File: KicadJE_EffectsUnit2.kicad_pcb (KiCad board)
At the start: 2 copper layers, 100 x 100 mm, 103 parts, among them J201 In_1, J202 In 2, J203 Out 1, J204 Out 2, J205 Out Final, J301 Conn_01x09_Male, J302 Conn_01x09_Male, J401 Conn_01x09_Male, J402 Conn_01x09_Male, P201 Doepfer_Power_10pin, P301 Doepfer_Power_10pin, SW201 Out 1, SW202 In or cascade, SW203 Out 2 FB, SW204 In or cascade, SW205 HI/LO, U201 TL072, U202 TL072, U401 TL072, U402 TL072

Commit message: 3D messing around
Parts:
- moved U402 60.2 mm to (120.0, 125.8), turned to 90 degrees
- moved C402 58.6 mm to (125.8, 73.1), turned to 90 degrees
- moved U401 55.5 mm to (120.0, 75.0), turned to 90 degrees
- moved C406 52.5 mm to (125.8, 77.0), turned to 90 degrees
- moved C405 47.9 mm to (125.0, 127.8), turned to 90 degrees
- moved C403 42.4 mm to (125.0, 123.8), turned to 90 degrees
- moved J402 1.42 mm to (128.0, 136.1)
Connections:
- C301 pad 1: -12V -> /angled_panel/-12V_1
- C301 pad 2: GND -> /angled_panel/GND_1
- C302 pad 1: GND -> /angled_panel/GND_1
- C302 pad 2: -12V -> /angled_panel/-12V_1
- C303 pad 1: GND -> /angled_panel/GND_1
- C303 pad 2: -12V -> /angled_panel/-12V_1
- C304 pad 1: GND -> /angled_panel/GND_1
- C304 pad 2: +12V -> /angled_panel/+12V_1
- C305 pad 1: +12V -> /angled_panel/+12V_1
- C305 pad 2: GND -> /angled_panel/GND_1
- C306 pad 1: +12V -> /angled_panel/+12V_1
- C306 pad 2: GND -> /angled_panel/GND_1
- C402 pad 2: Net-(C402-Pad2) -> +12V
- C403 pad 2: Net-(C402-Pad2) -> +12V
- C405 pad 1: Net-(C405-Pad1) -> -12V
- C406 pad 1: Net-(C405-Pad1) -> -12V
- D301 pad 1: -12V -> /angled_panel/-12V_1
- D301 pad 2: GND -> /angled_panel/GND_1
- D302 pad 1: GND -> /angled_panel/GND_1
- D302 pad 2: +12V -> /angled_panel/+12V_1
- J301 pad 1: /KicadJE_EU8_Dist/POT2_L -> /angled_panel/POT2_L
- J301 pad 2: /KicadJE_EU8_Dist/POT2_C -> /angled_panel/POT2_C
- J301 pad 3: /KicadJE_EU8_Dist/POT2_H -> /angled_panel/POT2_H
- J301 pad 4: -12V -> /angled_panel/-12V_1
- J301 pad 5: GND -> /angled_panel/GND_1
- J301 pad 6: +12V -> /angled_panel/+12V_1
- J301 pad 7: /KicadJE_EU8_Dist/POT1_L -> /angled_panel/POT1_L
- J301 pad 8: /KicadJE_EU8_Dist/POT1_C -> /angled_panel/POT1_C
- J301 pad 9: /KicadJE_EU8_Dist/POT1_H -> /angled_panel/POT1_H
- J302 pad 1: /KicadJE_EU8_Dist/POT4_L -> /angled_panel/POT4_L
- J302 pad 2: /KicadJE_EU8_Dist/POT4_C -> /angled_panel/POT4_C
- J302 pad 3: /KicadJE_EU8_Dist/POT4_H -> /angled_panel/POT4_H
- J302 pad 4: -12V -> /angled_panel/-12V_1
- J302 pad 5: GND -> /angled_panel/GND_1
- J302 pad 6: +12V -> /angled_panel/+12V_1
- J302 pad 7: /KicadJE_EU8_Dist/POT3_L -> /angled_panel/POT3_L
- J302 pad 8: /KicadJE_EU8_Dist/POT3_C -> /angled_panel/POT3_C
- J302 pad 9: /KicadJE_EU8_Dist/POT3_H -> /angled_panel/POT3_H
- J401 pad 1: /KicadJE_EU8_Dist/POT2_L -> (no net)
- J401 pad 2: /KicadJE_EU8_Dist/POT2_C -> (no net)
- J401 pad 3: /KicadJE_EU8_Dist/POT2_H -> (no net)
- J401 pad 7: /KicadJE_EU8_Dist/POT1_L -> (no net)
- J401 pad 8: /KicadJE_EU8_Dist/POT1_C -> (no net)
- J401 pad 9: /KicadJE_EU8_Dist/POT1_H -> (no net)
- J402 pad 1: /KicadJE_EU8_Dist/POT4_L -> (no net)
- J402 pad 2: /KicadJE_EU8_Dist/POT4_C -> (no net)
- J402 pad 3: /KicadJE_EU8_Dist/POT4_H -> (no net)
- J402 pad 7: /KicadJE_EU8_Dist/POT3_L -> (no net)
- J402 pad 8: /KicadJE_EU8_Dist/POT3_C -> (no net)
- J402 pad 9: /KicadJE_EU8_Dist/POT3_H -> (no net)
- P301 pad 1: -12V -> /angled_panel/-12V_1
- P301 pad 10: +12V -> /angled_panel/+12V_1
- P301 pad 2: -12V -> /angled_panel/-12V_1
- P301 pad 3: GND -> /angled_panel/GND_1
- P301 pad 4: GND -> /angled_panel/GND_1
- P301 pad 5: GND -> /angled_panel/GND_1
- P301 pad 6: GND -> /angled_panel/GND_1
- P301 pad 7: GND -> /angled_panel/GND_1
- P301 pad 8: GND -> /angled_panel/GND_1
- P301 pad 9: +12V -> /angled_panel/+12V_1
- RV301 pad 1: /KicadJE_EU8_Dist/POT1_L -> /angled_panel/POT1_L
- RV301 pad 2: /KicadJE_EU8_Dist/POT1_C -> /angled_panel/POT1_C
- RV301 pad 3: /KicadJE_EU8_Dist/POT1_H -> /angled_panel/POT1_H
- RV302 pad 1: /KicadJE_EU8_Dist/POT2_L -> /angled_panel/POT2_L
- RV302 pad 2: /KicadJE_EU8_Dist/POT2_C -> /angled_panel/POT2_C
- RV302 pad 3: /KicadJE_EU8_Dist/POT2_H -> /angled_panel/POT2_H
- RV303 pad 1: /KicadJE_EU8_Dist/POT3_L -> /angled_panel/POT3_L
- RV303 pad 2: /KicadJE_EU8_Dist/POT3_C -> /angled_panel/POT3_C
- RV303 pad 3: /KicadJE_EU8_Dist/POT3_H -> /angled_panel/POT3_H
- RV304 pad 1: /KicadJE_EU8_Dist/POT4_L -> /angled_panel/POT4_L
- RV304 pad 2: /KicadJE_EU8_Dist/POT4_C -> /angled_panel/POT4_C
- RV304 pad 3: /KicadJE_EU8_Dist/POT4_H -> /angled_panel/POT4_H
- U401 pad 4: Net-(C405-Pad1) -> -12V
- U401 pad 8: Net-(C402-Pad2) -> +12V
- U402 pad 4: Net-(C405-Pad1) -> -12V
- U402 pad 8: Net-(C402-Pad2) -> +12V
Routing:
- net /angled_panel/+12V_1: track 0.00 -> 116.8 mm, vias 0 -> 4
- net +12V: track 116.8 -> 12.8 mm, vias 4 -> 0
- net /angled_panel/-12V_1: track 0.00 -> 83.5 mm
- net -12V: track 83.5 -> 23.2 mm
- net /angled_panel/GND_1: track 0.00 -> 36.1 mm, vias 0 -> 50
- net GND: track 94.2 -> 72.1 mm, vias 133 -> 84
- net /angled_panel/POT2_L: track 0.00 -> 11.2 mm
- net /KicadJE_EU8_Dist/POT2_L: track 11.2 -> 0.00 mm
- net /angled_panel/POT3_H: track 0.00 -> 10.9 mm
- net /KicadJE_EU8_Dist/POT3_H: track 10.9 -> 0.00 mm
- net /angled_panel/POT2_C: track 0.00 -> 8.74 mm
- net /KicadJE_EU8_Dist/POT2_C: track 8.74 -> 0.00 mm
- net /angled_panel/POT3_C: track 0.00 -> 8.42 mm
- net /KicadJE_EU8_Dist/POT3_C: track 8.42 -> 0.00 mm
- net /angled_panel/POT2_H: track 0.00 -> 6.28 mm
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- added copper zone on B.Cu, net /angled_panel/GND_1
- added copper zone on F.Cu, net /angled_panel/GND_1
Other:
- outline, holes or cut-outs redrawn

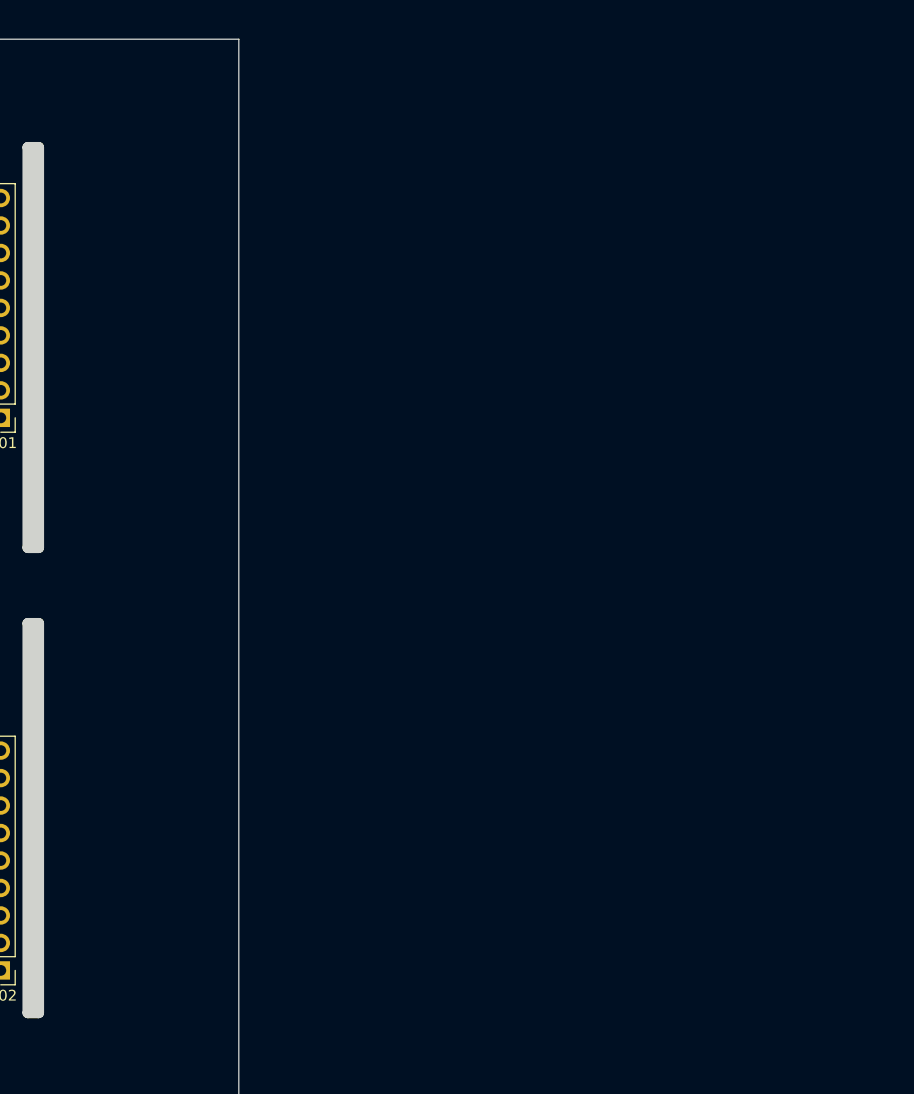
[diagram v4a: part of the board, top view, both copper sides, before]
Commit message: PCB dist 2 placement of face panel
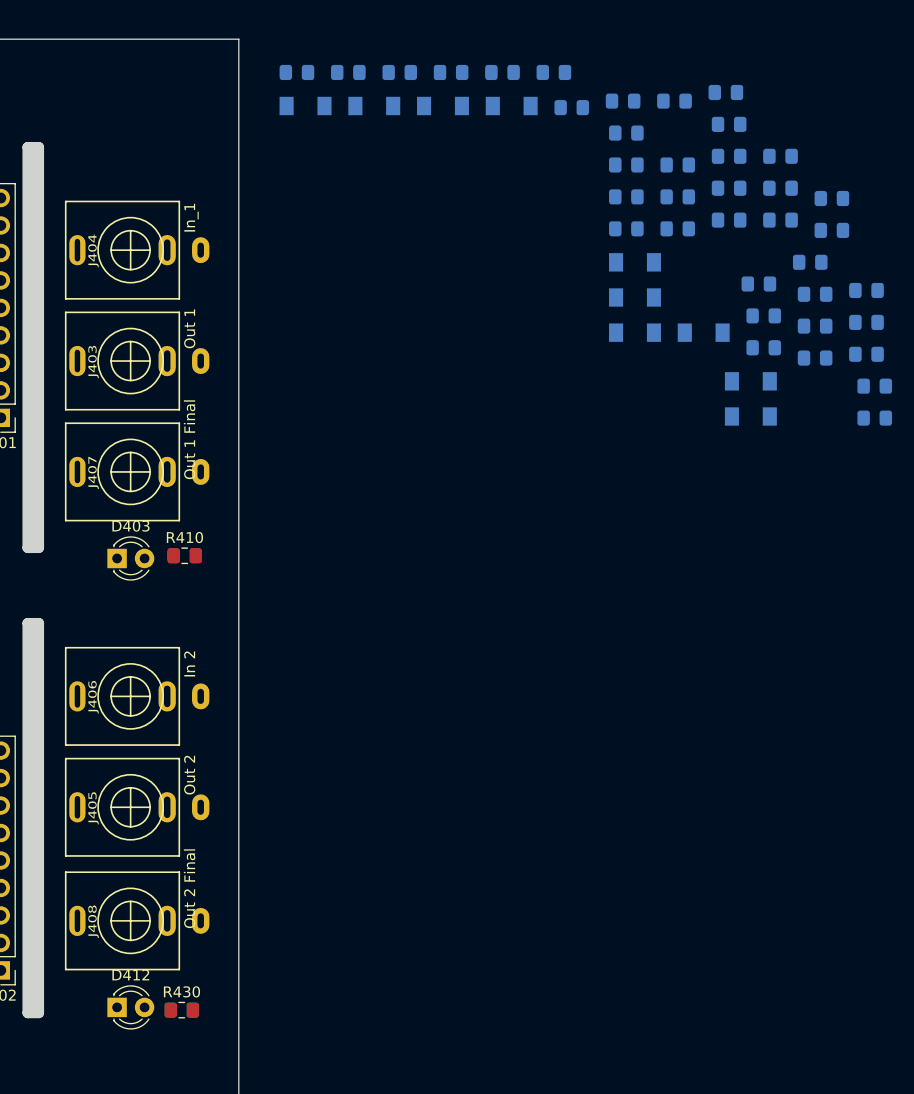
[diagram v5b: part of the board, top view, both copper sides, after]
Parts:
- added C401: 10n, Capacitor_SMD:C_0805_2012Metric_Pad1.15x1.40mm_HandSolder, B.Cu at (198.5, 75.6)
- added C404: 10n, Capacitor_SMD:C_0805_2012Metric_Pad1.15x1.40mm_HandSolder, B.Cu at (164.9, 53.1)
- added C407: 10n, Capacitor_SMD:C_0805_2012Metric_Pad1.15x1.40mm_HandSolder, B.Cu at (169.6, 53.1)
- added C408: 10n, Capacitor_SMD:C_0805_2012Metric_Pad1.15x1.40mm_HandSolder, B.Cu at (198.5, 78.5)
- added C409: 1u, Capacitor_SMD:C_0805_2012Metric_Pad1.15x1.40mm_HandSolder, B.Cu at (185.8, 67.5)
- added C410: 1u, Capacitor_SMD:C_0805_2012Metric_Pad1.15x1.40mm_HandSolder, B.Cu at (185.8, 64.6)
- added C411: 1u, Capacitor_SMD:C_0805_2012Metric_Pad1.15x1.40mm_HandSolder, B.Cu at (174.4, 53.1)
- added C412: 1u, Capacitor_SMD:C_0805_2012Metric_Pad1.15x1.40mm_HandSolder, B.Cu at (155.4, 53.1)
- added C413: 1u, Capacitor_SMD:C_0805_2012Metric_Pad1.15x1.40mm_HandSolder, B.Cu at (180.8, 56.3)
- added C414: 1u, Capacitor_SMD:C_0805_2012Metric_Pad1.15x1.40mm_HandSolder, B.Cu at (185.8, 61.6)
- added D401: LL4148, Diode_SMD:D_MiniMELF, B.Cu at (186.6, 77.1)
- added D402: LL4148, Diode_SMD:D_MiniMELF, B.Cu at (168.9, 56.2)
- added D403: LED, LED_THT:LED_D3.0mm, F.Cu at (138.8, 98.0)
- added D404: LL4148, Diode_SMD:D_MiniMELF, B.Cu at (193.0, 77.1)
- added D405: LL4148, Diode_SMD:D_MiniMELF, B.Cu at (156.2, 56.2)
- added D406: LL4148, Diode_SMD:D_MiniMELF, B.Cu at (162.5, 56.2)
- added D407: LL4148, Diode_SMD:D_MiniMELF, B.Cu at (186.6, 73.9)
- added D408: LL4148, Diode_SMD:D_MiniMELF, B.Cu at (175.2, 56.2)
- added D409: LL4148, Diode_SMD:D_MiniMELF, B.Cu at (197.3, 84.9)
- added D410: D_Zener, Diode_SMD:D_MiniMELF, B.Cu at (186.6, 70.6)
- added D411: D_Zener, Diode_SMD:D_MiniMELF, B.Cu at (197.3, 81.6)
- added D412: LED, LED_THT:LED_D3.0mm, F.Cu at (138.8, 139.5)
- added J403: Out 1, AJ-Dropbox-Kicad:PJ301SM, F.Cu at (140.0, 79.8)
- added J404: In_1, AJ-Dropbox-Kicad:PJ301SM, F.Cu at (140.0, 69.5)
- added J405: Out 2, AJ-Dropbox-Kicad:PJ301SM, F.Cu at (140.0, 121.0)
- added J406: In 2, AJ-Dropbox-Kicad:PJ301SM, F.Cu at (140.0, 110.8)
- added J407: Out 1 Final, AJ-Dropbox-Kicad:PJ301SM, F.Cu at (140.0, 90.0)
- added J408: Out 2 Final, AJ-Dropbox-Kicad:PJ301SM, F.Cu at (140.0, 131.5)
- added R401: 1k, Resistor_SMD:R_0805_2012Metric_Pad1.15x1.40mm_HandSolder, B.Cu at (190.6, 67.5)
- added R402: 10k, Resistor_SMD:R_0805_2012Metric_Pad1.15x1.40mm_HandSolder, B.Cu at (208.0, 76.2)
- added R403: 10k, Resistor_SMD:R_0805_2012Metric_Pad1.15x1.40mm_HandSolder, B.Cu at (203.3, 79.5)
- added R404: 1k, Resistor_SMD:R_0805_2012Metric_Pad1.15x1.40mm_HandSolder, B.Cu at (190.6, 64.6)
- added R405: 1k, Resistor_SMD:R_0805_2012Metric_Pad1.15x1.40mm_HandSolder, B.Cu at (198.1, 72.6)
- added R406: 1k, Resistor_SMD:R_0805_2012Metric_Pad1.15x1.40mm_HandSolder, B.Cu at (179.1, 53.1)
- added R407: 10k, Resistor_SMD:R_0805_2012Metric_Pad1.15x1.40mm_HandSolder, B.Cu at (203.3, 76.5)
- added R408: 10k, Resistor_SMD:R_0805_2012Metric_Pad1.15x1.40mm_HandSolder, B.Cu at (208.8, 82.1)
- added R409: 10R, Resistor_SMD:R_0805_2012Metric_Pad1.15x1.40mm_HandSolder, B.Cu at (185.8, 58.7)
- added R410: 1k, Resistor_SMD:R_0805_2012Metric_Pad1.15x1.40mm_HandSolder, F.Cu at (145.0, 97.8)
- added R411: 1k, Resistor_SMD:R_0805_2012Metric_Pad1.15x1.40mm_HandSolder, B.Cu at (190.6, 61.6)
- added R412: 10k, Resistor_SMD:R_0805_2012Metric_Pad1.15x1.40mm_HandSolder, B.Cu at (195.3, 66.7)
- added R413: 10k, Resistor_SMD:R_0805_2012Metric_Pad1.15x1.40mm_HandSolder, B.Cu at (185.5, 55.7)
- added R414: 1k, Resistor_SMD:R_0805_2012Metric_Pad1.15x1.40mm_HandSolder, B.Cu at (208.0, 79.1)
- added R415: 10k, Resistor_SMD:R_0805_2012Metric_Pad1.15x1.40mm_HandSolder, B.Cu at (203.3, 73.6)
- added R416: 10k, Resistor_SMD:R_0805_2012Metric_Pad1.15x1.40mm_HandSolder, B.Cu at (208.8, 85.0)
- added R417: 1k, Resistor_SMD:R_0805_2012Metric_Pad1.15x1.40mm_HandSolder, B.Cu at (160.1, 53.1)
- added R418: Open, Resistor_SMD:R_0805_2012Metric_Pad1.15x1.40mm_HandSolder, B.Cu at (195.3, 63.8)
- added R419: Open, Resistor_SMD:R_0805_2012Metric_Pad1.15x1.40mm_HandSolder, B.Cu at (202.8, 70.6)
- added R420: 1k, Resistor_SMD:R_0805_2012Metric_Pad1.15x1.40mm_HandSolder, B.Cu at (200.1, 66.7)
- added R421: 10R, Resistor_SMD:R_0805_2012Metric_Pad1.15x1.40mm_HandSolder, B.Cu at (190.3, 55.7)
- added R422: 0R, Resistor_SMD:R_0805_2012Metric_Pad1.15x1.40mm_HandSolder, B.Cu at (195.3, 60.8)
- added R423: 0R, Resistor_SMD:R_0805_2012Metric_Pad1.15x1.40mm_HandSolder, B.Cu at (208.0, 73.2)
- added R424: 10k, Resistor_SMD:R_0805_2012Metric_Pad1.15x1.40mm_HandSolder, B.Cu at (200.1, 63.8)
- added R425: OPEN, Resistor_SMD:R_0805_2012Metric_Pad1.15x1.40mm_HandSolder, B.Cu at (204.8, 67.7)
- added R426: 10k, Resistor_SMD:R_0805_2012Metric_Pad1.15x1.40mm_HandSolder, B.Cu at (195.3, 57.9)
- added R427: OPEN, Resistor_SMD:R_0805_2012Metric_Pad1.15x1.40mm_HandSolder, B.Cu at (200.1, 60.8)
- added R428: 100k, Resistor_SMD:R_0805_2012Metric_Pad1.15x1.40mm_HandSolder, B.Cu at (204.8, 64.7)
- added R429: 100k, Resistor_SMD:R_0805_2012Metric_Pad1.15x1.40mm_HandSolder, B.Cu at (195.0, 54.9)
- added R430: 1k, Resistor_SMD:R_0805_2012Metric_Pad1.15x1.40mm_HandSolder, F.Cu at (144.7, 139.8)
- R209, R214: value 150R -> 680R
- R216: value 1k -> 10R
- R220: value 150R -> 1k
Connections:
- J401 pad 1: (no net) -> /KicadJE_EU8_Dist/POT2_L
- J401 pad 2: (no net) -> /KicadJE_EU8_Dist/POT2_C
- J401 pad 3: (no net) -> /KicadJE_EU8_Dist/POT2_C
- J401 pad 7: (no net) -> /KicadJE_EU8_Dist/POT1_L
- J401 pad 8: (no net) -> /KicadJE_EU8_Dist/POT1_C
- J401 pad 9: (no net) -> /KicadJE_EU8_Dist/POT1_C
- J402 pad 1: (no net) -> /KicadJE_EU8_Dist/POT4_L
- J402 pad 2: (no net) -> /KicadJE_EU8_Dist/POT4_C
- J402 pad 3: (no net) -> /KicadJE_EU8_Dist/POT4_C
- J402 pad 7: (no net) -> /KicadJE_EU8_Dist/POT3_L
- J402 pad 8: (no net) -> /KicadJE_EU8_Dist/POT3_C
- J402 pad 9: (no net) -> /KicadJE_EU8_Dist/POT3_C
- U401 pad 1: (no net) -> Net-(R405-Pad2)
- U401 pad 2: (no net) -> /KicadJE_EU8_Dist/POT1_L
- U401 pad 3: (no net) -> Net-(R407-Pad1)
- U401 pad 5: (no net) -> Net-(R408-Pad1)
- U401 pad 6: (no net) -> /KicadJE_EU8_Dist/POT2_L
- U401 pad 7: (no net) -> Net-(R404-Pad2)
- U402 pad 1: (no net) -> /KicadJE_EU8_Dist/POT3_C
- U402 pad 2: (no net) -> Net-(C407-Pad1)
- U402 pad 3: (no net) -> Net-(R418-Pad1)
- U402 pad 5: (no net) -> Net-(R419-Pad1)
- U402 pad 6: (no net) -> Net-(R413-Pad2)
- U402 pad 7: (no net) -> /KicadJE_EU8_Dist/POT4_C

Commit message: Update KicadJE_EffectsUnit2.kicad_pcb
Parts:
- moved R430 4.46 mm to (149.0, 138.5), turned to 90 degrees
- moved R410 4.07 mm to (149.0, 97.0), turned to 90 degrees
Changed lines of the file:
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@@
   )
   (module Resistor_SMD:R_0805_2012Metric_Pad1.15x1.40mm_HandSolder (layer F.Cu)
-    (at 145 97.75)
-    (descr "Resistor SMD 0805 (2012 Metric), square (rectangular) end terminal, IPC_7351 nominal with elongated pad for handsoldering. (Body size source: https://docs.google.com/spreadsheets/d/1BsfQQcO9C6DZCsRaXUlFlo91Tg2WpOkGARC1WS5S8t0/edit?usp=sharing), generated with kicad-footprint-generator")
-    (tags "resistor handsolder")
-    (attr smd)
-    (fp_text reference R410 (at 0 -1.65) (layer F.SilkS)
+    (at 149 96.975 90)
+    (descr "Resistor SMD 0805 (2012 Metric), square (rectangular) end terminal, IPC_7351 nominal with elongated pad for handsoldering. (Body size source: https://docs.google.com/spreadsheets/d/1BsfQQcO9C6DZCsRaXUlFlo91Tg2WpOkGARC1WS5S8t0/edit?usp=sharing), generated with kicad-footprint-generator")
+    (tags "resistor handsolder")
+    (attr smd)
+    (fp_text reference R410 (at 0 -1.65 90) (layer F.SilkS)
       (effects (font (size 1 1) (thickness 0.15)))
     )
-    (fp_text value 1k (at 0 1.65) (layer F.Fab)
+    (fp_text value 1k (at -3 0 90) (layer F.Fab)
       (effects (font (size 1 1) (thickness 0.15)))
     )
-    (fp_text user %R (at 0 0) (layer F.Fab)
+    (fp_text user %R (at 0 0 90) (layer F.Fab)
       (effects (font (size 0.5 0.5) (thickness 0.08)))
     )
@@
     (fp_line (start -1 -0.6) (end 1 -0.6) (layer F.Fab) (width 0.1))
     (fp_line (start -1 0.6) (end -1 -0.6) (layer F.Fab) (width 0.1))
-    (pad 2 smd roundrect (at 1.025 0) (size 1.15 1.4) (layers F.Cu F.Paste F.Mask) (roundrect_rratio 0.217391)
+    (pad 2 smd roundrect (at 1.025 0 90) (size 1.15 1.4) (layers F.Cu F.Paste F.Mask) (roundrect_rratio 0.217391)
       (net 81 "Net-(R404-Pad2)"))
-    (pad 1 smd roundrect (at -1.025 0) (size 1.15 1.4) (layers F.Cu F.Paste F.Mask) (roundrect_rratio 0.217391)
+    (pad 1 smd roundrect (at -1.025 0 90) (size 1.15 1.4) (layers F.Cu F.Paste F.Mask) (roundrect_rratio 0.217391)
       (net 70 "Net-(D403-Pad2)"))
     (model ${KISYS3DMOD}/Resistor_SMD.3dshapes/R_0805_2012Metric.wrl
@@
   )
   (module Resistor_SMD:R_0805_2012Metric_Pad1.15x1.40mm_HandSolder (layer F.Cu)
-    (at 144.725 139.75)
-    (descr "Resistor SMD 0805 (2012 Metric), square (rectangular) end terminal, IPC_7351 nominal with elongated pad for handsoldering. (Body size source: https://docs.google.com/spreadsheets/d/1BsfQQcO9C6DZCsRaXUlFlo91Tg2WpOkGARC1WS5S8t0/edit?usp=sharing), generated with kicad-footprint-generator")
-    (tags "resistor handsolder")
-    (attr smd)
-    (fp_text reference R430 (at 0 -1.65) (layer F.SilkS)
+    (at 149 138.475 90)
+    (descr "Resistor SMD 0805 (2012 Metric), square (rectangular) end terminal, IPC_7351 nominal with elongated pad for handsoldering. (Body size source: https://docs.google.com/spreadsheets/d/1BsfQQcO9C6DZCsRaXUlFlo91Tg2WpOkGARC1WS5S8t0/edit?usp=sharing), generated with kicad-footprint-generator")
+    (tags "resistor handsolder")
+    (attr smd)
+    (fp_text reference R430 (at 0 -1.65 90) (layer F.SilkS)
       (effects (font (size 1 1) (thickness 0.15)))
     )
-    (fp_text value 1k (at 0 1.65) (layer F.Fab)
+    (fp_text value 1k (at -3.5 0 90) (layer F.Fab)
       (effects (font (size 1 1) (thickness 0.15)))
     )
-    (fp_text user %R (at 0 0) (layer F.Fab)
+    (fp_text user %R (at -0.25 0.25 90) (layer F.Fab)
       (effects (font (size 0.5 0.5) (thickness 0.08)))
     )
@@
     (fp_line (start -1 -0.6) (end 1 -0.6) (layer F.Fab) (width 0.1))
     (fp_line (start -1 0.6) (end -1 -0.6) (layer F.Fab) (width 0.1))
-    (pad 2 smd roundrect (at 1.025 0) (size 1.15 1.4) (layers F.Cu F.Paste F.Mask) (roundrect_rratio 0.217391)
+    (pad 2 smd roundrect (at 1.025 0 90) (size 1.15 1.4) (layers F.Cu F.Paste F.Mask) (roundrect_rratio 0.217391)
       (net 76 /KicadJE_EU8_Dist/POT4_C))
-    (pad 1 smd roundrect (at -1.025 0) (size 1.15 1.4) (layers F.Cu F.Paste F.Mask) (roundrect_rratio 0.217391)
+    (pad 1 smd roundrect (at -1.025 0 90) (size 1.15 1.4) (layers F.Cu F.Paste F.Mask) (roundrect_rratio 0.217391)
       (net 71 "Net-(D412-Pad2)"))
     (model ${KISYS3DMOD}/Resistor_SMD.3dshapes/R_0805_2012Metric.wrl

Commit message: Update KicadJE_EffectsUnit2.kicad_pcb
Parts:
- moved H302 123.6 mm to (94.5, 147.0)
- moved H303 108.8 mm to (105.5, 147.0)
- moved H401 43.2 mm to (125.1, 40.5)
- moved H402 43.2 mm to (131.6, 40.5)
- moved H301 22.9 mm to (94.5, 53.0)
- moved H304 21.8 mm to (105.5, 53.0)
- moved C304 2.50 mm to (92.5, 59.5)
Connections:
- net Out1Final renamed Out1_Final
- net Out2Final renamed Out2_Final
- C409 pad 2: Out1Dist -> Out1_Dist
- C410 pad 2: In1 -> In_1
- C411 pad 2: Out2Dist -> Out2_Dist
- C412 pad 2: In2 -> In_2
- R407 pad 2: In1 -> In_1
- R411 pad 2: Out1Dist -> Out1_Dist
- R415 pad 2: In2 -> In_2
- R420 pad 2: Out2Dist -> Out2_Dist
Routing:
- net Net-(J404-PadT): track 0.00 -> 59.5 mm
- net /angled_panel/+12V_1: track 116.8 -> 107.7 mm

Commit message: Update KicadJE_EffectsUnit2.kicad_pcb
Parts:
- moved R424 74.0 mm to (140.0, 107.0), turned to 180 degrees
- moved R407 72.9 mm to (135.5, 103.5)
- moved R425 72.0 mm to (144.5, 107.0)
- moved C410 65.8 mm to (135.5, 107.0), turned to 180 degrees
- moved D410 61.7 mm to (139.5, 110.5)
- moved D404 53.5 mm to (165.0, 31.5), turned to 180 degrees
- moved D411 32.1 mm to (207.0, 51.0)
- moved D402 30.7 mm to (187.0, 81.0), turned to 180 degrees
- moved R429 26.2 mm to (169.5, 49.0)
- moved D407 20.8 mm to (169.5, 62.0)
- moved D408 19.7 mm to (191.5, 45.0), turned to 180 degrees
- moved D405 16.7 mm to (165.0, 42.0)
- moved C404 15.6 mm to (164.9, 37.5), turned to 180 degrees
- moved R421 12.9 mm to (197.5, 45.0)
- moved R426 9.58 mm to (202.0, 51.0)
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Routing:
- net Net-(R407-Pad1): track 0.00 -> 31.5 mm
- net Net-(C410-Pad1): track 0.00 -> 12.2 mm
- net GND: track 72.1 -> 79.9 mm
- net Net-(J404-PadT): track 59.5 -> 64.2 mm
- net In_1: track 0.00 -> 4.35 mm
